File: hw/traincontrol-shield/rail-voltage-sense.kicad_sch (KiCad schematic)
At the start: 2 parts

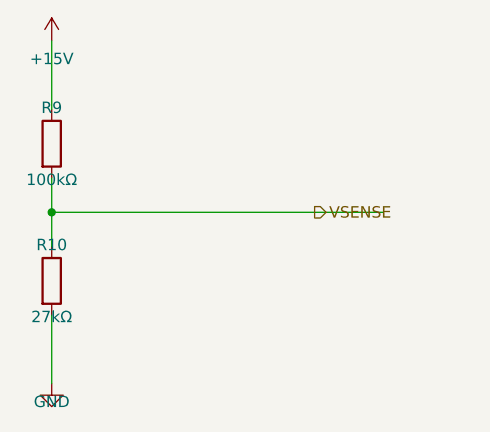
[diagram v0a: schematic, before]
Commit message: Fix hlabel placement: label sits at stub outer end (lx), not pin tip (x)
The hierarchical label connection point must be at lx (the outer end of
the stub wire), not at x (the IC pin tip). With the label at x, it was
overlapping the pin itself instead of sitting at the end of the routing
stub where it belongs.

  angle=180 (left-side): lx = x - STUB  → label to the left of pin ✓
  angle=0   (right-side): lx = x + STUB  → label to the right of pin ✓

Wire still runs x↔lx, connecting the IC pin to the label connection.
Updated gen_all_sheets.py and gen_power_supply.py.

Co-Authored-By: Claude Sonnet 4.6 <noreply@anthropic.com>
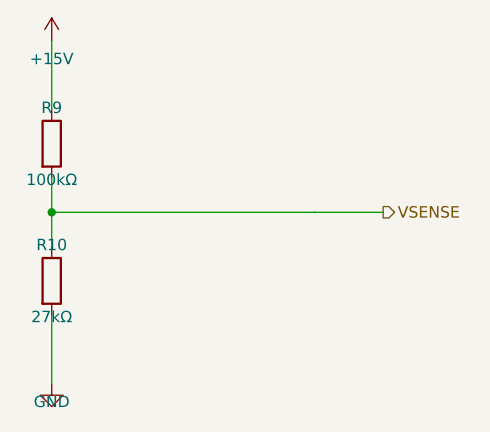
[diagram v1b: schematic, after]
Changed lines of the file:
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@@
 	(hierarchical_label "VSENSE"
 		(shape output)
-		(at 109.22 83.82 0)
+		(at 116.84 83.82 0)
 		(fields_autoplaced yes)
 		(effects (font (size 1.27 1.27)) (justify left bottom))
 		(property "Intersheetrefs" "${INTERSHEET_REFS}"
-			(at 109.22 83.82 0)
+			(at 116.84 83.82 0)
 			(effects (font (size 1.27 1.27)) (hide yes))
 		)
